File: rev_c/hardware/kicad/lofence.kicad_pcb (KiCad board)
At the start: 2 copper layers, 78 x 130 mm, 61 parts, among them J1 Fence+, J2 Fence-, J3 ISP, J4 DEBUG RN, J5 DEBUG LED, J6 DEBUG MCU, J7 868, SW1 RESET, U1 Opamp_Dual_Generic, U3 ATmega328PB-AU, U4 RN2483, U5 MCP125x, Y1 32768 Hz

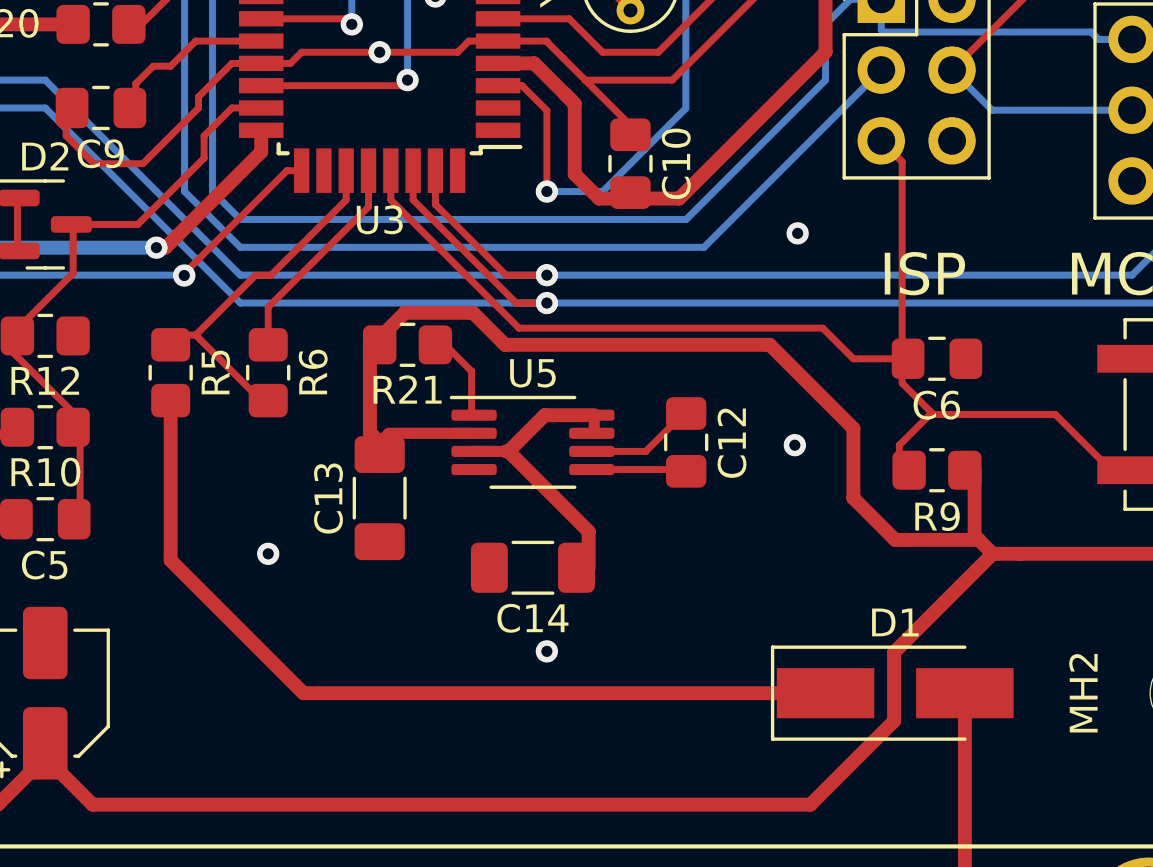
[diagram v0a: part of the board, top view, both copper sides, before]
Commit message: fix battery power
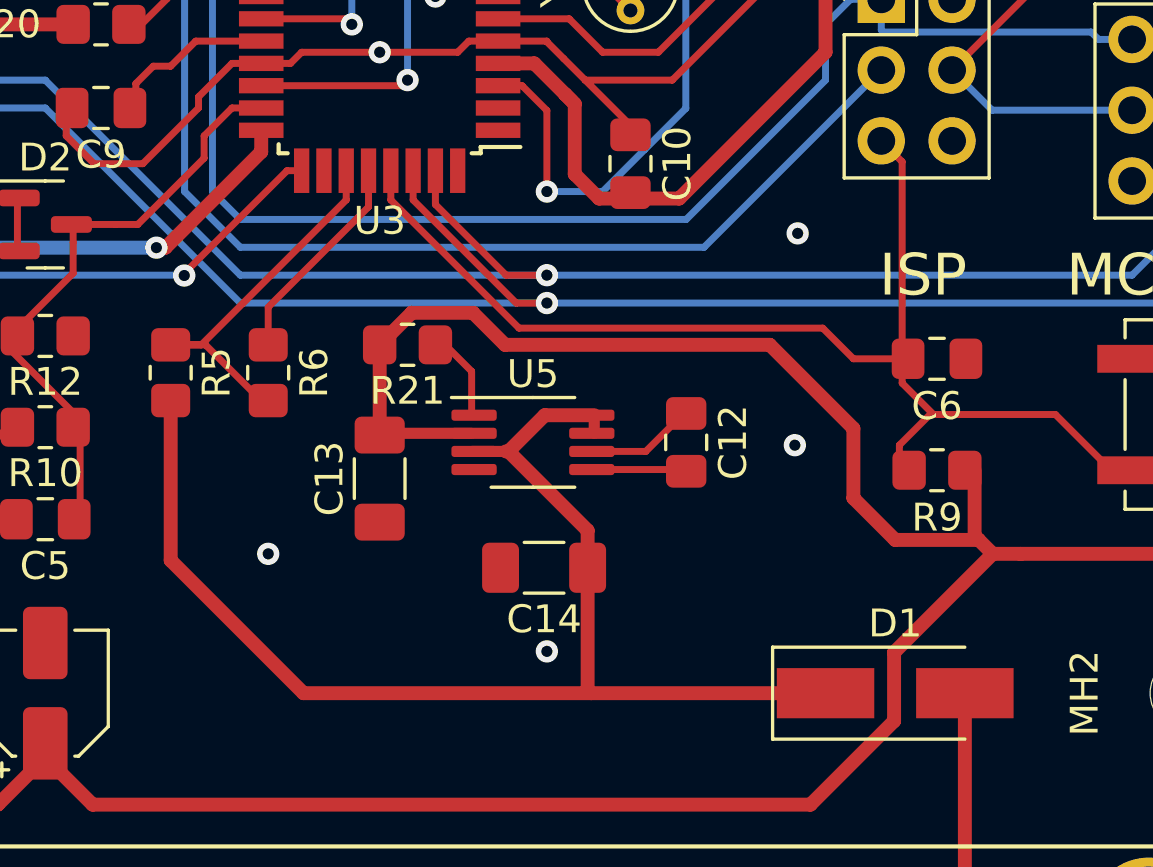
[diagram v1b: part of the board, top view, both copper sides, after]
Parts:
- moved C13 0.70 mm to (74.0, 94.3)
- moved C14 0.40 mm to (79.9, 97.5)
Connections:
- C14 pad 1: VCC_BBC -> BAT_VCC
- U5 pad 3: VCC_BBC -> BAT_VCC
- U5 pad 7: VCC_BBC -> BAT_VCC
- U5 pad 8: VCC_BBC -> BAT_VCC
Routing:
- net BAT_VCC: track 30.9 -> 46.4 mm
- net VCC_BBC: track 11.0 -> 0.00 mm
- net BAT_ADC: track 13.0 -> 14.3 mm
- net +3V3: track 302.5 -> 301.6 mm
